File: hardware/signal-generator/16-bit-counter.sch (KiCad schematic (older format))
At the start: 8 parts, among them U1 74HC04, U13 74HC4040, U14 74HC4040, U2 74HC08, U3 74HC08, U4 74HC30

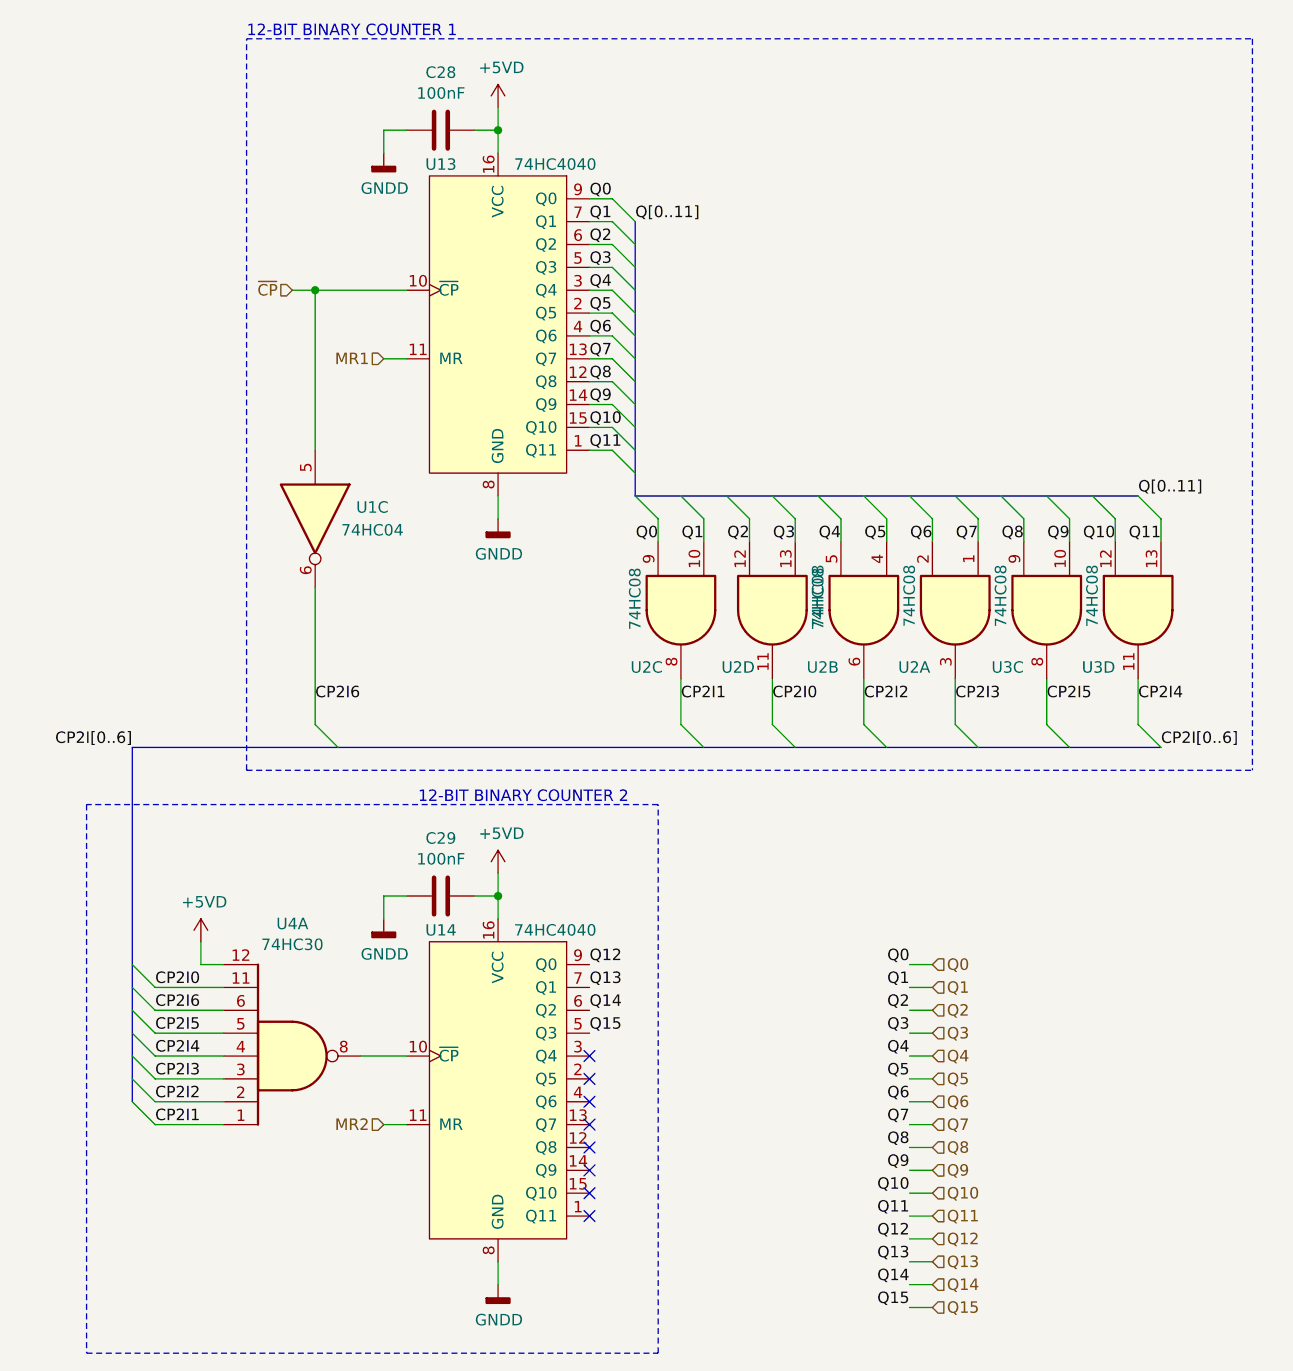
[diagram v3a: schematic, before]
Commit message: [Signal Generator] Rework DDS system PCB layout
The previous layout of the DDS system had its components rather
awkwardly positioned. Furthermore, it did not take into account the
distinction of the digital and analog grounds, as well as their star
ground connection.
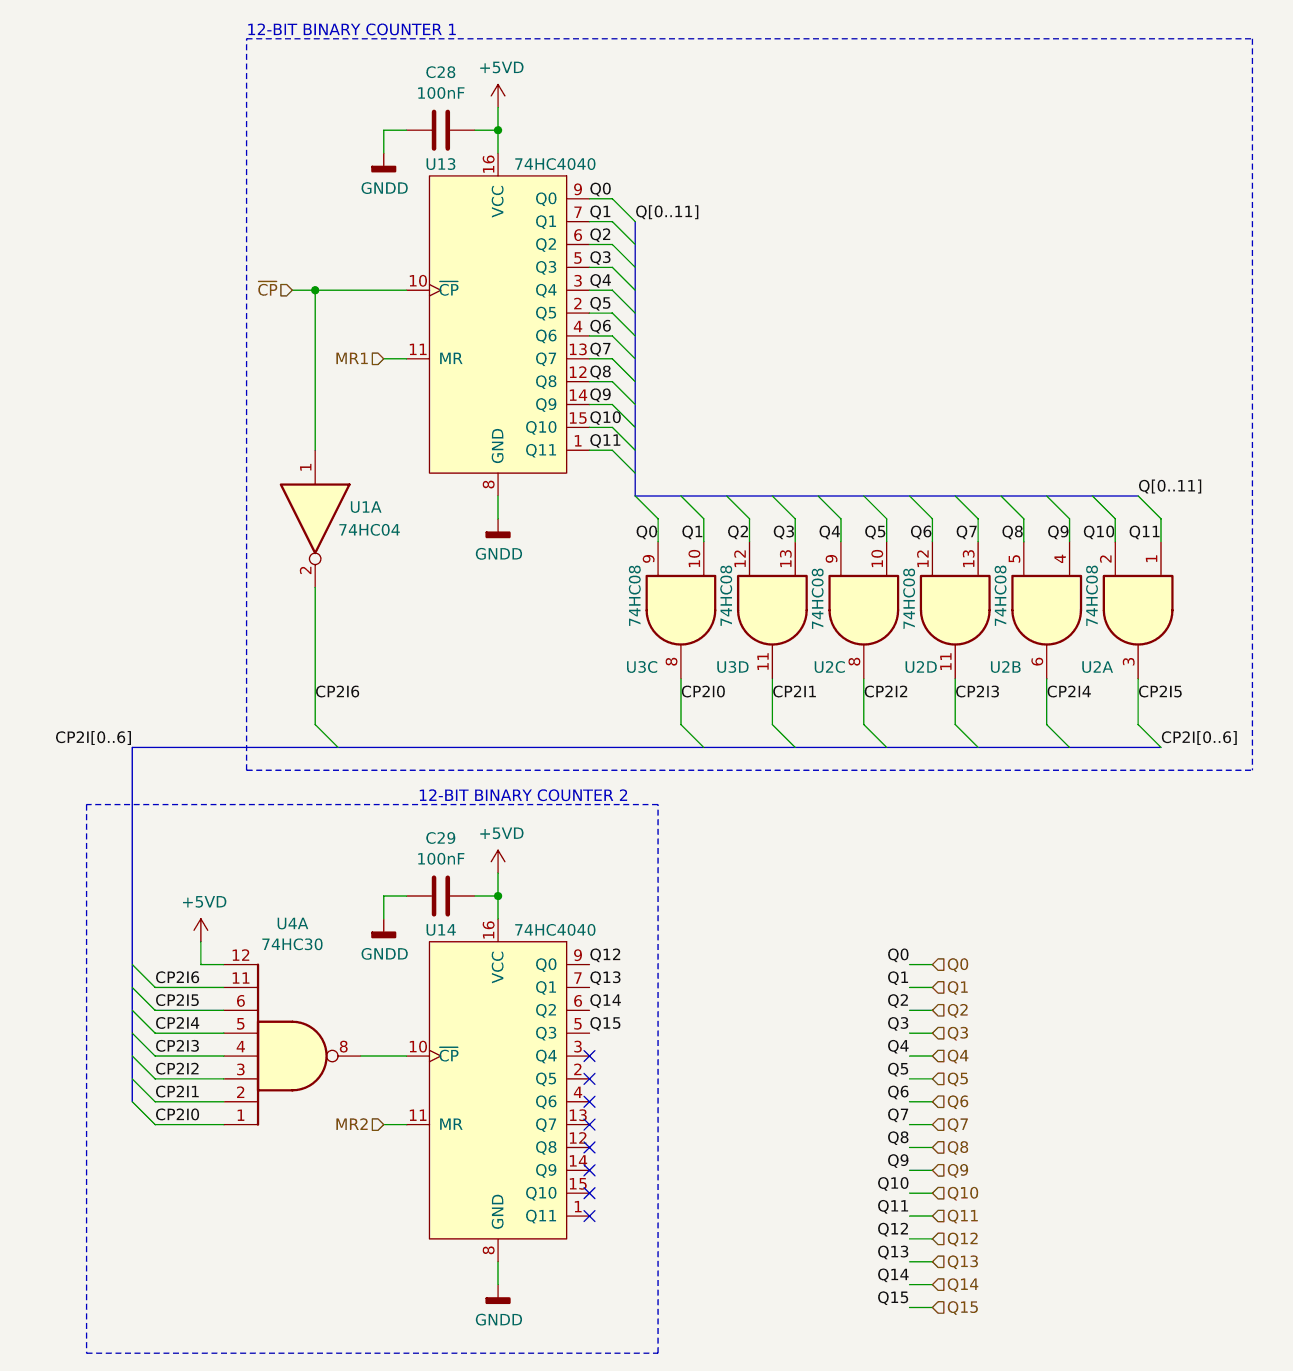
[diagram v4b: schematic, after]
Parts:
- removed U1: 74HC04, Housings_SOIC:SOIC-14_3.9x8.7mm_Pitch1.27mm, symbol 74xx:74HC04
- added U1: 74HC04, Housings_SOIC:SOIC-14_3.9x8.7mm_Pitch1.27mm, symbol 74xx:74HC04
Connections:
- net CP2I0: now also U3.8, U4.1; no longer U2.11, U4.11
- net CP2I1: now also U3.11, U4.2; no longer U2.8, U4.1
- net CP2I2: now also U2.8, U4.3; no longer U2.6, U4.2
- net CP2I3: now also U2.11, U4.4; no longer U2.3, U4.3
- net CP2I4: now also U2.6, U4.5; no longer U3.11, U4.4
- net CP2I5: now also U2.3, U4.6; no longer U3.8, U4.5
- net CP2I6: now also U4.11, U1.2; no longer U4.6
- net Q0: now also U3.9; no longer U2.9
- net Q1: now also U3.10; no longer U2.10
- net Q10: now also U2.2; no longer U3.12
- net Q11: now also U2.1; no longer U3.13
- net Q2: now also U3.12; no longer U2.12
- net Q3: now also U3.13; no longer U2.13
- net Q4: now also U2.9; no longer U2.5
- net Q5: now also U2.10; no longer U2.4
- net Q6: now also U2.12; no longer U2.2
- net Q7: now also U2.13; no longer U2.1
- net Q8: now also U2.5; no longer U3.9
- net Q9: now also U2.4; no longer U3.10
- net ~CP: now also U1.1
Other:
- moved on the sheet: U2A, U2B, U2C, U2D, U3C, U3D
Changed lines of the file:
@@
 Sheet 3 5
 Title "Digital Function Generator v2 - DDS 16-bit counter"
-Date "2019-12-26"
+Date "2019-12-28"
 Rev "1"
 Comp "Petar Nikolov"
@@
 Text HLabel 3750 5600 0    50   Input ~ 0
 MR2
+Text Label 2750 5600 0    50   ~ 0
+CP2I0
+Text Label 2750 5500 0    50   ~ 0
+CP2I1
+Text Label 2750 5400 0    50   ~ 0
+CP2I2
+Text Label 2750 5300 0    50   ~ 0
+CP2I3
+Text Label 2750 5200 0    50   ~ 0
+CP2I4
+Text Label 2750 5100 0    50   ~ 0
+CP2I5
 Text Label 2750 5000 0    50   ~ 0
-CP2I0
-Text Label 2750 5600 0    50   ~ 0
-CP2I1
-Text Label 2750 5500 0    50   ~ 0
-CP2I2
-Text Label 2750 5400 0    50   ~ 0
-CP2I3
-Text Label 2750 5300 0    50   ~ 0
-CP2I4
-Text Label 2750 5200 0    50   ~ 0
-CP2I5
-Text Label 2750 5100 0    50   ~ 0
 CP2I6
 Text Label 2650 3950 2    50   ~ 0
 CP2I[0..6]
+Text Label 5050 3750 0    50   ~ 0
+CP2I0
 Text Label 5450 3750 0    50   ~ 0
-CP2I0
-Text Label 5050 3750 0    50   ~ 0
 CP2I1
 Text Label 5850 3750 0    50   ~ 0
@@
 Text Label 6250 3750 0    50   ~ 0
 CP2I3
+Text Label 6650 3750 0    50   ~ 0
+CP2I4
 Text Label 7050 3750 0    50   ~ 0
-CP2I4
-Text Label 6650 3750 0    50   ~ 0
 CP2I5
 Text Label 3450 3750 0    50   ~ 0
@@
 L ulib_MY_74xx:74HC08 U2
 U 2 1 5DDE89F7
-P 5850 3350
-F 0 "U2" V 6100 3100 50  0000 L CNN
-F 1 "74HC08" H 5650 3150 50  0000 L CNN
-F 2 "Housings_SOIC:SOIC-14_3.9x8.7mm_Pitch1.27mm" H 5850 3300 50  0001 C CNN
-F 3 "https://assets.nexperia.com/documents/data-sheet/74HC_HCT08.pdf" H 5850 3400 50  0001 C CNN
-	2    5850 3350
+P 6650 3350
+F 0 "U2" V 6900 3100 50  0000 L CNN
+F 1 "74HC08" H 6450 3150 50  0000 L CNN
+F 2 "Housings_SOIC:SOIC-14_3.9x8.7mm_Pitch1.27mm" H 6650 3300 50  0001 C CNN
+F 3 "https://assets.nexperia.com/documents/data-sheet/74HC_HCT08.pdf" H 6650 3400 50  0001 C CNN
+	2    6650 3350
 	0    1    1    0
 $EndComp
@@
 L ulib_MY_74xx:74HC08 U3
 U 3 1 5DDE8B26
-P 6650 3350
-F 0 "U3" V 6900 3450 50  0000 L CNN
-F 1 "74HC08" H 6450 3550 50  0000 L CNN
-F 2 "Housings_SOIC:SOIC-14_3.9x8.7mm_Pitch1.27mm" H 6650 3300 50  0001 C CNN
-F 3 "https://assets.nexperia.com/documents/data-sheet/74HC_HCT08.pdf" H 6650 3400 50  0001 C CNN
-	3    6650 3350
+P 5050 3350
+F 0 "U3" V 5300 3450 50  0000 L CNN
+F 1 "74HC08" H 4850 3550 50  0000 L CNN
+F 2 "Housings_SOIC:SOIC-14_3.9x8.7mm_Pitch1.27mm" H 5050 3300 50  0001 C CNN
+F 3 "https://assets.nexperia.com/documents/data-sheet/74HC_HCT08.pdf" H 5050 3400 50  0001 C CNN
+	3    5050 3350
 	0    -1   1    0
 $EndComp
@@
 L ulib_MY_74xx:74HC08 U3
 U 4 1 5DDE8C64
-P 7050 3350
-F 0 "U3" V 7300 3450 50  0000 L CNN
-F 1 "74HC08" H 6850 3550 50  0000 L CNN
-F 2 "Housings_SOIC:SOIC-14_3.9x8.7mm_Pitch1.27mm" H 7050 3300 50  0001 C CNN
-F 3 "https://assets.nexperia.com/documents/data-sheet/74HC_HCT08.pdf" H 7050 3400 50  0001 C CNN
-	4    7050 3350
-	0    -1   1    0
-$EndComp
-$Comp
-L ulib_MY_74xx:74HC08 U2
-U 4 1 5E0FAF21
 P 5450 3350
-AR Path="/5DB72CF6/5DBBB708/5E0FAF21" Ref="U2"  Part="4"
-AR Path="/5DE65B3D/5E0FAF21" Ref="U?"  Part="4"
-AR Path="/5E0FAF21" Ref="U?"  Part="4"
-F 0 "U2" V 5700 3500 50  0000 C CNN
-F 1 "74HC08" H 5400 3150 50  0000 C CNN
+F 0 "U3" V 5700 3450 50  0000 L CNN
+F 1 "74HC08" H 5250 3550 50  0000 L CNN
 F 2 "Housings_SOIC:SOIC-14_3.9x8.7mm_Pitch1.27mm" H 5450 3300 50  0001 C CNN
 F 3 "https://assets.nexperia.com/documents/data-sheet/74HC_HCT08.pdf" H 5450 3400 50  0001 C CNN
@@
 $Comp
 L ulib_MY_74xx:74HC08 U2
+U 4 1 5E0FAF21
+P 6250 3350
+AR Path="/5DB72CF6/5DBBB708/5E0FAF21" Ref="U2"  Part="4"
+AR Path="/5DE65B3D/5E0FAF21" Ref="U?"  Part="4"
+AR Path="/5E0FAF21" Ref="U?"  Part="4"
+F 0 "U2" V 6500 3500 50  0000 C CNN
+F 1 "74HC08" H 6200 3550 50  0000 C CNN
+F 2 "Housings_SOIC:SOIC-14_3.9x8.7mm_Pitch1.27mm" H 6250 3300 50  0001 C CNN
+F 3 "https://assets.nexperia.com/documents/data-sheet/74HC_HCT08.pdf" H 6250 3400 50  0001 C CNN
+	4    6250 3350
+	0    -1   1    0
+$EndComp
+$Comp
+L ulib_MY_74xx:74HC08 U2
 U 3 1 5E137EE3
-P 5050 3350
+P 5850 3350
 AR Path="/5DB72CF6/5DBBB708/5E137EE3" Ref="U2"  Part="3"
 AR Path="/5DE65B3D/5E137EE3" Ref="U?"  Part="3"
 AR Path="/5E137EE3" Ref="U?"  Part="3"
-F 0 "U2" V 5300 3500 50  0000 C CNN
-F 1 "74HC08" H 5000 3550 50  0000 C CNN
-F 2 "Housings_SOIC:SOIC-14_3.9x8.7mm_Pitch1.27mm" H 5050 3300 50  0001 C CNN
-F 3 "https://assets.nexperia.com/documents/data-sheet/74HC_HCT08.pdf" H 5050 3400 50  0001 C CNN
-	3    5050 3350
+F 0 "U2" V 6100 3500 50  0000 C CNN
+F 1 "74HC08" H 5800 3550 50  0000 C CNN
+F 2 "Housings_SOIC:SOIC-14_3.9x8.7mm_Pitch1.27mm" H 5850 3300 50  0001 C CNN
+F 3 "https://assets.nexperia.com/documents/data-sheet/74HC_HCT08.pdf" H 5850 3400 50  0001 C CNN
+	3    5850 3350
 	0    -1   1    0
 $EndComp
@@
 L ulib_MY_74xx:74HC08 U2
 U 1 1 5DDE88D1
-P 6250 3350
-F 0 "U2" V 6500 3100 50  0000 L CNN
-F 1 "74HC08" H 6050 3150 50  0000 L CNN
-F 2 "Housings_SOIC:SOIC-14_3.9x8.7mm_Pitch1.27mm" H 6250 3300 50  0001 C CNN
-F 3 "https://assets.nexperia.com/documents/data-sheet/74HC_HCT08.pdf" H 6250 3400 50  0001 C CNN
-	1    6250 3350
+P 7050 3350
+F 0 "U2" V 7300 3100 50  0000 L CNN
+F 1 "74HC08" H 6850 3150 50  0000 L CNN
+F 2 "Housings_SOIC:SOIC-14_3.9x8.7mm_Pitch1.27mm" H 7050 3300 50  0001 C CNN
+F 3 "https://assets.nexperia.com/documents/data-sheet/74HC_HCT08.pdf" H 7050 3400 50  0001 C CNN
+	1    7050 3350
 	0    1    1    0
 $EndComp
 $Comp
-L 74xx:74HC04 U?
-U 3 1 5E4488E7
+L 74xx:74HC04 U1
+U 1 1 5E0C4B22
 P 3450 2950
-AR Path="/5E4488E7" Ref="U?"  Part="3"
-AR Path="/5DB72CF6/5DBBB708/5E4488E7" Ref="U1"  Part="3"
-F 0 "U1" V 3400 3200 50  0000 C CNN
-F 1 "74HC04" V 3500 3200 50  0000 C CNN
+AR Path="/5DB72CF6/5DBBB708/5E0C4B22" Ref="U1"  Part="1"
+AR Path="/5E0C4B22" Ref="U?"  Part="1"
+F 0 "U1" V 3400 3100 50  0000 L CNN
+F 1 "74HC04" V 3500 3050 50  0000 L CNN
 F 2 "Housings_SOIC:SOIC-14_3.9x8.7mm_Pitch1.27mm" H 3450 2950 50  0001 C CNN
 F 3 "https://assets.nexperia.com/documents/data-sheet/74HC_HCT04.pdf" H 3450 2950 50  0001 C CNN
-	3    3450 2950
+	1    3450 2950
 	0    1    1    0
 $EndComp

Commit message: [Signal Generator] Restore PCB layout with new symbol annotations
The new components have been loaded in the PCB file.
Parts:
- renumbered U3 to U2, U2 to U3
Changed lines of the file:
@@
 $EndComp
 $Comp
-L ulib_MY_74xx:74HC08 U2
+L ulib_MY_74xx:74HC08 U3
 U 2 1 5DDE89F7
 P 6650 3350
-F 0 "U2" V 6900 3100 50  0000 L CNN
+F 0 "U3" V 6900 3100 50  0000 L CNN
 F 1 "74HC08" H 6450 3150 50  0000 L CNN
 F 2 "Housings_SOIC:SOIC-14_3.9x8.7mm_Pitch1.27mm" H 6650 3300 50  0001 C CNN
@@
 $EndComp
 $Comp
-L ulib_MY_74xx:74HC08 U3
+L ulib_MY_74xx:74HC08 U2
 U 3 1 5DDE8B26
 P 5050 3350
-F 0 "U3" V 5300 3450 50  0000 L CNN
+F 0 "U2" V 5300 3450 50  0000 L CNN
 F 1 "74HC08" H 4850 3550 50  0000 L CNN
 F 2 "Housings_SOIC:SOIC-14_3.9x8.7mm_Pitch1.27mm" H 5050 3300 50  0001 C CNN
@@
 $EndComp
 $Comp
-L ulib_MY_74xx:74HC08 U3
+L ulib_MY_74xx:74HC08 U2
 U 4 1 5DDE8C64
 P 5450 3350
-F 0 "U3" V 5700 3450 50  0000 L CNN
+F 0 "U2" V 5700 3450 50  0000 L CNN
 F 1 "74HC08" H 5250 3550 50  0000 L CNN
 F 2 "Housings_SOIC:SOIC-14_3.9x8.7mm_Pitch1.27mm" H 5450 3300 50  0001 C CNN
@@
 $EndComp
 $Comp
-L ulib_MY_74xx:74HC08 U2
+L ulib_MY_74xx:74HC08 U3
 U 4 1 5E0FAF21
 P 6250 3350
-AR Path="/5DB72CF6/5DBBB708/5E0FAF21" Ref="U2"  Part="4"
+AR Path="/5DB72CF6/5DBBB708/5E0FAF21" Ref="U3"  Part="4"
 AR Path="/5DE65B3D/5E0FAF21" Ref="U?"  Part="4"
 AR Path="/5E0FAF21" Ref="U?"  Part="4"
-F 0 "U2" V 6500 3500 50  0000 C CNN
+F 0 "U3" V 6500 3500 50  0000 C CNN
 F 1 "74HC08" H 6200 3550 50  0000 C CNN
 F 2 "Housings_SOIC:SOIC-14_3.9x8.7mm_Pitch1.27mm" H 6250 3300 50  0001 C CNN
@@
 $EndComp
 $Comp
-L ulib_MY_74xx:74HC08 U2
+L ulib_MY_74xx:74HC08 U3
 U 3 1 5E137EE3
 P 5850 3350
-AR Path="/5DB72CF6/5DBBB708/5E137EE3" Ref="U2"  Part="3"
+AR Path="/5DB72CF6/5DBBB708/5E137EE3" Ref="U3"  Part="3"
 AR Path="/5DE65B3D/5E137EE3" Ref="U?"  Part="3"
 AR Path="/5E137EE3" Ref="U?"  Part="3"
-F 0 "U2" V 6100 3500 50  0000 C CNN
+F 0 "U3" V 6100 3500 50  0000 C CNN
 F 1 "74HC08" H 5800 3550 50  0000 C CNN
 F 2 "Housings_SOIC:SOIC-14_3.9x8.7mm_Pitch1.27mm" H 5850 3300 50  0001 C CNN
@@
 $EndComp
 $Comp
-L ulib_MY_74xx:74HC08 U2
+L ulib_MY_74xx:74HC08 U3
 U 1 1 5DDE88D1
 P 7050 3350
-F 0 "U2" V 7300 3100 50  0000 L CNN
+F 0 "U3" V 7300 3100 50  0000 L CNN
 F 1 "74HC08" H 6850 3150 50  0000 L CNN
 F 2 "Housings_SOIC:SOIC-14_3.9x8.7mm_Pitch1.27mm" H 7050 3300 50  0001 C CNN
